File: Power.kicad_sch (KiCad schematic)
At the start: 13 parts, among them J2 EuroPower10_THT, U3 TL072, U4 TL072

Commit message: add gerbers and bom
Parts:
- C1, C2, C3, C8, C9: LCSC (none) -> C14663
- C4, C5, C6: LCSC (none) -> C15850; LCSC PN C15850 -> (none)
- D2, D3: LCSC (none) -> C191023; LCSC PN C191023 -> (none)
- J2: JLCPCB_IGNORE (none) -> 1
- U3, U4: LCSC (none) -> C6961; LCSC PN C6961 -> (none)
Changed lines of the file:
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@@
 			)
 		)
-		(property "LCSC PN" "C191023"
+		(property "LCSC" "C191023"
+			(at 53.34 43.18 0)
+			(effects
+				(font
+					(size 1.27 1.27)
+				)
+				(hide yes)
+			)
+		)
+		(property "JLCPCB_IGNORE" ""
 			(at 53.34 43.18 0)
 			(effects
@@
 			)
 		)
-		(property "LCSC PN" "C6961"
+		(property "LCSC" "C6961"
+			(at 118.11 49.53 0)
+			(effects
+				(font
+					(size 1.27 1.27)
+				)
+				(hide yes)
+			)
+		)
+		(property "JLCPCB_IGNORE" ""
 			(at 118.11 49.53 0)
 			(effects
@@
 			)
 		)
-		(property "LCSC PN" "C15850"
+		(property "LCSC" "C15850"
+			(at 66.04 52.07 0)
+			(effects
+				(font
+					(size 1.27 1.27)
+				)
+				(hide yes)
+			)
+		)
+		(property "JLCPCB_IGNORE" ""
 			(at 66.04 52.07 0)
 			(effects
@@
 			)
 		)
-		(property "LCSC PN" ""
+		(property "LCSC" "C14663"
+			(at 142.24 53.34 0)
+			(effects
+				(font
+					(size 1.27 1.27)
+				)
+				(hide yes)
+			)
+		)
+		(property "JLCPCB_IGNORE" ""
 			(at 142.24 53.34 0)
 			(effects
@@
 			)
 		)
+		(property "JLCPCB_IGNORE" "1"
+			(at 43.18 43.18 0)
+			(effects
+				(font
+					(size 1.27 1.27)
+				)
+				(hide yes)
+			)
+		)
 		(pin "5"
 		)
@@
 			)
 		)
-		(property "LCSC PN" ""
+		(property "LCSC" "C14663"
+			(at 88.9 48.26 0)
+			(effects
+				(font
+					(size 1.27 1.27)
+				)
+				(hide yes)
+			)
+		)
+		(property "JLCPCB_IGNORE" ""
 			(at 88.9 48.26 0)
 			(effects
@@
 			)
 		)
-		(property "LCSC PN" "C6961"
+		(property "LCSC" "C6961"
+			(at 135.89 49.53 0)
+			(effects
+				(font
+					(size 1.27 1.27)
+				)
+				(hide yes)
+			)
+		)
+		(property "JLCPCB_IGNORE" ""
 			(at 135.89 49.53 0)
 			(effects
@@
 			)
 		)
-		(property "LCSC PN" ""
+		(property "LCSC" "C14663"
+			(at 142.24 45.72 0)
+			(effects
+				(font
+					(size 1.27 1.27)
+				)
+				(hide yes)
+			)
+		)
+		(property "JLCPCB_IGNORE" ""
 			(at 142.24 45.72 0)
 			(effects
@@
 			)
 		)
-		(property "LCSC PN" "C15850"
+		(property "LCSC" "C15850"
+			(at 66.04 44.45 0)
+			(effects
+				(font
+					(size 1.27 1.27)
+				)
+				(hide yes)
+			)
+		)
+		(property "JLCPCB_IGNORE" ""
 			(at 66.04 44.45 0)
 			(effects
@@
 			)
 		)
-		(property "LCSC PN" ""
+		(property "LCSC" "C14663"
+			(at 123.19 53.34 0)
+			(effects
+				(font
+					(size 1.27 1.27)
+				)
+				(hide yes)
+			)
+		)
+		(property "JLCPCB_IGNORE" ""
 			(at 123.19 53.34 0)
 			(effects
@@
 			)
 		)
-		(property "LCSC PN" ""
+		(property "LCSC" "C14663"
+			(at 123.19 45.72 0)
+			(effects
+				(font
+					(size 1.27 1.27)
+				)
+				(hide yes)
+			)
+		)
+		(property "JLCPCB_IGNORE" ""
 			(at 123.19 45.72 0)
 			(effects
@@
 			)
 		)
-		(property "LCSC PN" "C191023"
+		(property "LCSC" "C191023"
+			(at 53.34 53.34 0)
+			(effects
+				(font
+					(size 1.27 1.27)
+				)
+				(hide yes)
+			)
+		)
+		(property "JLCPCB_IGNORE" ""
 			(at 53.34 53.34 0)
 			(effects
@@
 			)
 		)
-		(property "LCSC PN" "C15850"
+		(property "LCSC" "C15850"
 			(at 106.68 48.26 0)
 			(effects
+				(font
+					(size 1.27 1.27)
+				)
+				(hide yes)
+			)
+		)
+		(property "JLCPCB_IGNORE" ""
+			(at 106.68 48.26 0)
+			(effects

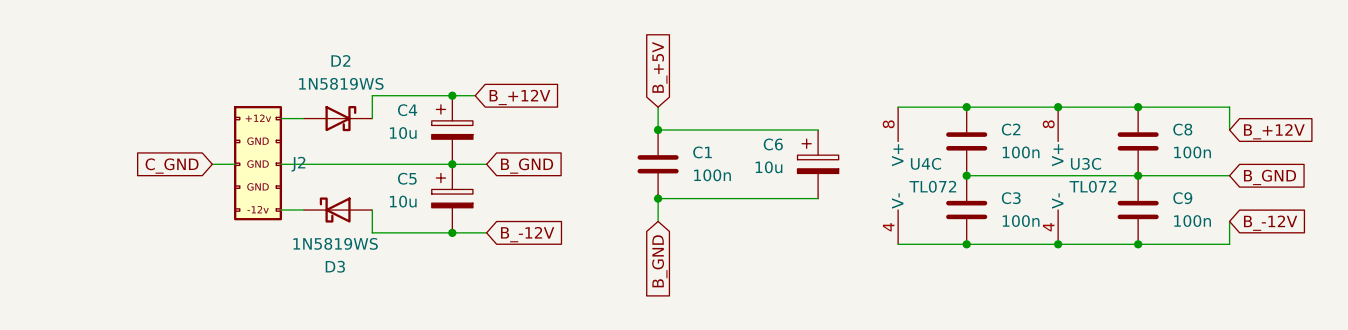
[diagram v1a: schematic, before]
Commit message: add rev 2 and rev 3, now with correct trs midi A
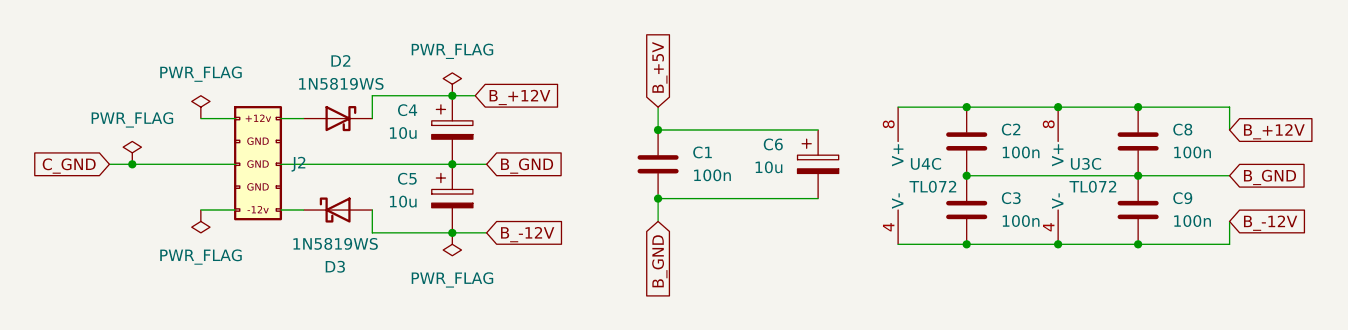
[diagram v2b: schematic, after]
